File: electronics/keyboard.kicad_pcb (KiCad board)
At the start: 2 copper layers, 169 parts, among them J1 CONN_02X10, SW1 SW_Push, SW10 SW_Push, SW11 SW_Push, SW12 SW_Push, SW13 SW_Push, SW14 SW_Push, SW15 SW_Push, SW16 SW_Push, SW17 SW_Push, SW18 SW_Push, SW19 SW_Push, SW20 SW_Push, SW21 SW_Push, SW22 SW_Push, SW23 SW_Push, SW24 SW_Push, SW25 SW_Push, SW27 SW_Push, SW28 SW_Push, SW29 SW_Push, SW3 SW_Push, SW30 SW_Push, SW31 SW_Push, SW32 SW_Push, SW33 SW_Push, SW34 SW_Push, SW35 SW_Push, SW36 SW_Push, SW37 SW_Push, SW38 SW_Push, SW39 SW_Push, SW4 SW_Push, SW40 SW_Push, SW41 SW_Push, SW42 SW_Push, SW43 SW_Push, SW44 SW_Push, SW45 SW_Push, SW46 SW_Push, SW47 SW_Push, SW48 SW_Push, SW49 SW_Push, SW5 SW_Push, SW50 SW_Push, SW51 SW_Push, SW52 SW_Push, SW53 SW_Push, SW54 SW_Push, SW55 SW_Push, SW56 SW_Push, SW57 SW_Push, SW58 SW_Push, SW59 SW_Push, SW6 SW_Push, SW60 SW_Push, SW61 SW_Push, SW62 SW_Push, SW63 SW_Push, SW64 SW_Push, SW65 SW_Push, SW66 SW_Push, SW67 SW_Push, SW68 SW_Push, SW69 SW_Push, SW7 SW_Push, SW70 SW_Push, SW71 SW_Push, SW72 SW_Push, SW73 SW_Push, SW74 SW_Push, SW75 SW_Push, SW76 SW_Push, SW77 SW_Push, SW78 SW_Push, SW8 SW_Push, SW81 SW_Push, SW82 SW_Push, SW83 SW_Push, SW84 SW_Push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

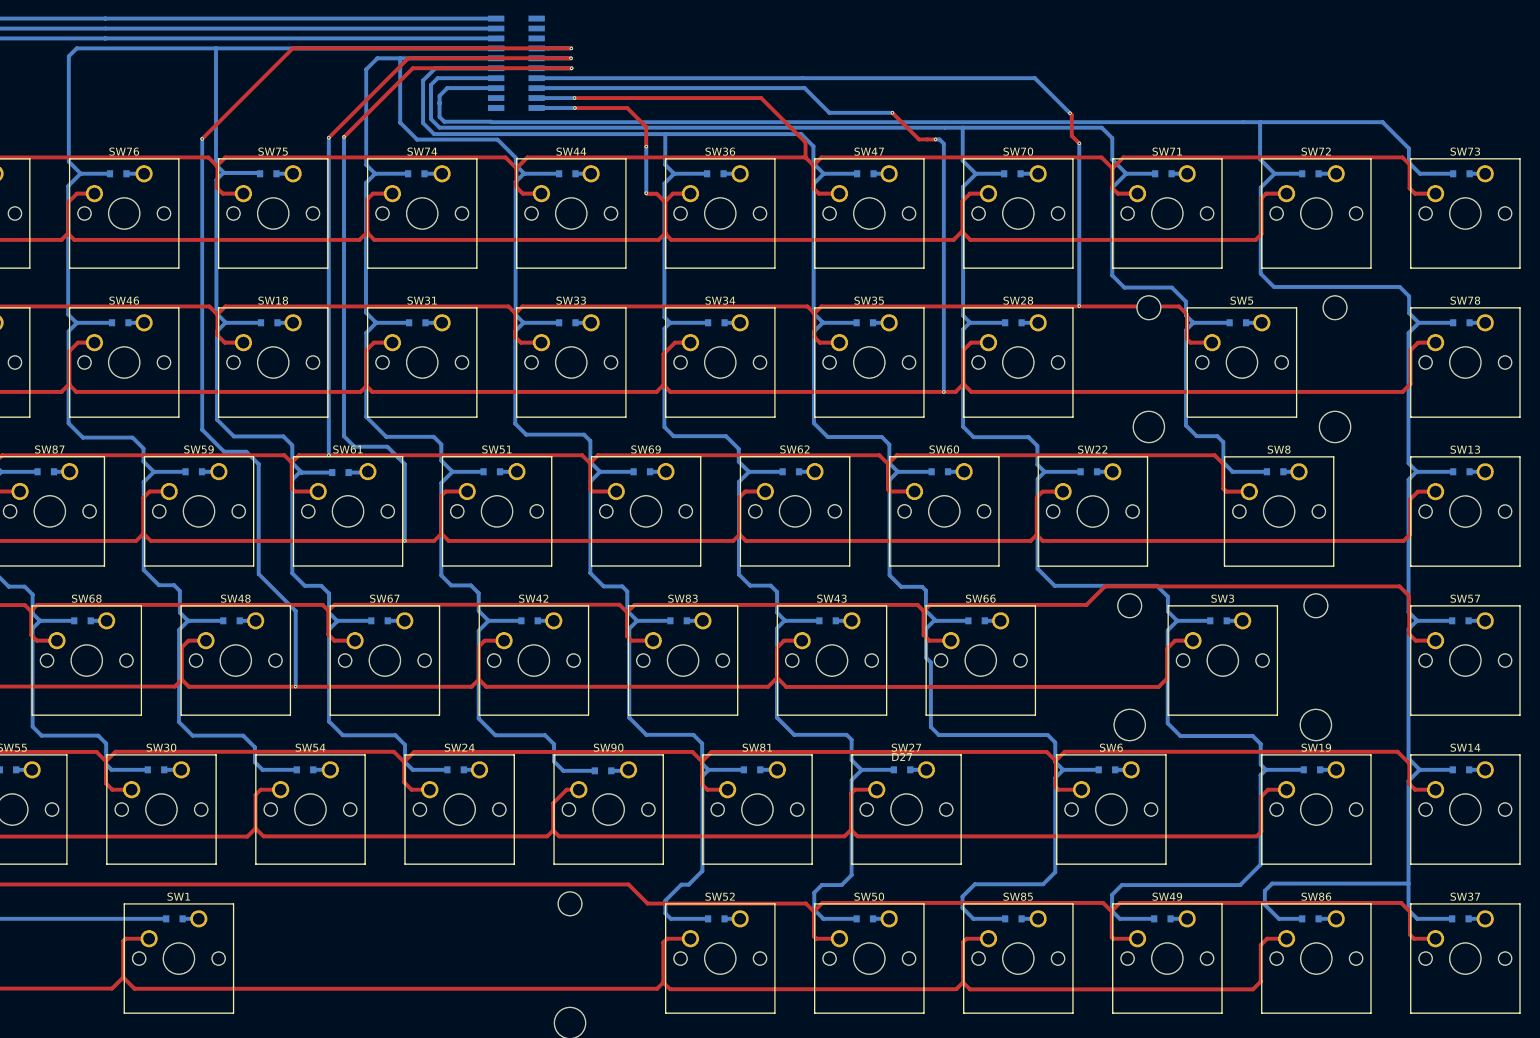
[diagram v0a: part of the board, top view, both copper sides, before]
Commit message: Initial complete signal routing of the connector
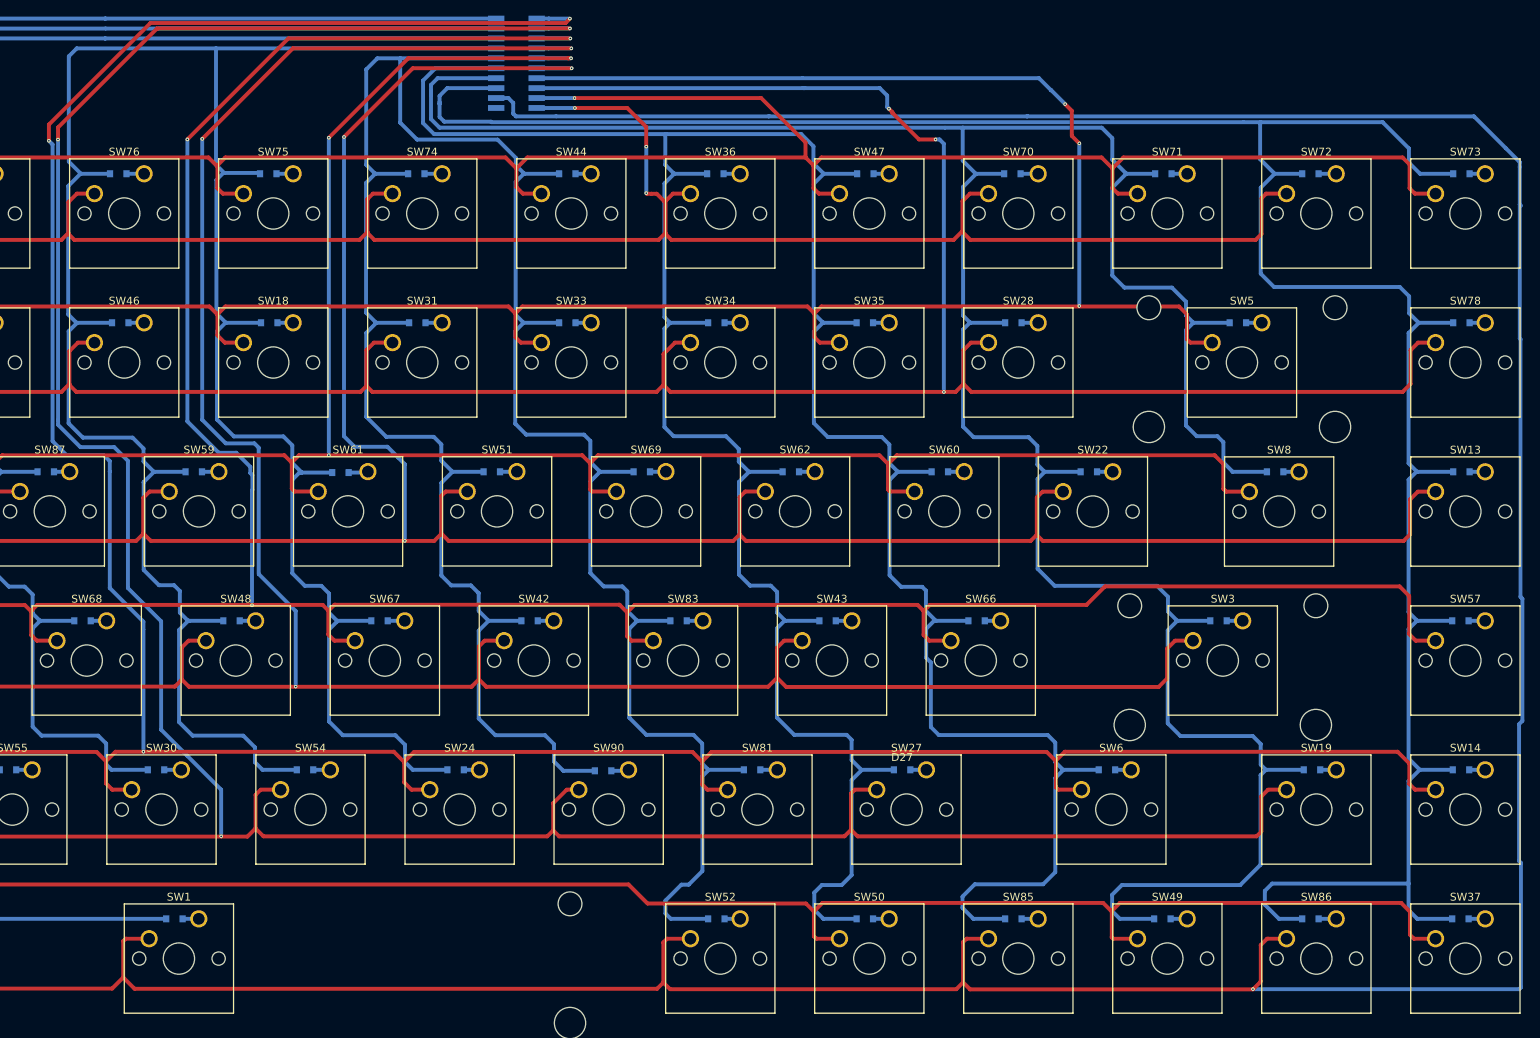
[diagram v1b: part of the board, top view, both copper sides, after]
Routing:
- net /PC2: track 318.7 -> 594.3 mm, vias 0 -> 1
- net /PC0: track 313.9 -> 490.7 mm, vias 0 -> 3
- net /PC1: track 294.9 -> 459.3 mm, vias 0 -> 3
- net /PB7: track 306.4 -> 429.4 mm, vias 0 -> 3
- net /PB2: track 442.0 -> 443.1 mm

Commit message: Fixed strange drc errors with replacing vias
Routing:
- net /PB2: track 443.1 -> 447.2 mm
- net Net-(D58-Pad2): track 0.00 -> 2.01 mm
- net /PA0: track 545.5 -> 547.5 mm
- net /PC0: track 490.7 -> 492.3 mm
- net /PB7: track 429.4 -> 430.2 mm
- net /PB6: track 438.8 -> 439.5 mm
- net /PC1: track 459.3 -> 459.9 mm

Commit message: Added outline and some drill holes
todo:
    - Additional 2 drill holes
    - update fill zones
    - add led for shift switch
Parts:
- added REF**: MountingHole_3.2mm_M3, Mounting_Holes:MountingHole_3.2mm_M3, F.Cu at (34.9, 228.0)
- added REF**: MountingHole_3.2mm_M3, Mounting_Holes:MountingHole_3.2mm_M3, F.Cu at (320.9, 228.0)
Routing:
- net /PA1: track 465.7 -> 456.9 mm
- added copper zone on B.Cu, net (none)
- added copper zone on F.Cu, net (none)
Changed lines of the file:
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@@
 (kicad_pcb (version 4) (host pcbnew 4.0.6)
   (general
-    (links 251)
-    (no_connects 1)
-    (area 25.703749 90 331.110001 225.07)
+    (links 0)
+    (no_connects 0)
+    (area 25.350857 89.714399 331.110001 234.128001)
     (thickness 1.6)
-    (drawings 1853)
+    (drawings 1856)
     (tracks 1422)
     (zones 0)
-    (modules 169)
+    (modules 171)
     (nets 106)
   )
@@
     (33 F.Adhes user)
     (34 B.Paste user)
-    (35 F.Paste user)
+    (35 F.Paste user hide)
     (36 B.SilkS user)
     (37 F.SilkS user)
@@
     (pad_drill 0.762)
     (pad_to_mask_clearance 0.2)
-    (aux_axis_origin 0 0)
-    (visible_elements FFFFF77F)
+    (aux_axis_origin 25.908 224.028)
+    (grid_origin 25.908 224.028)
+    (visible_elements FFFFFFFF)
     (pcbplotparams
       (layerselection 0x00030_80000001)
@@
     (add_net "Net-(D90-Pad2)")
   )
+  (module Mounting_Holes:MountingHole_3.2mm_M3 (layer F.Cu)
+    (at 34.908 228.028)
+    (descr "Mounting Hole 3.2mm, no annular, M3")
+    (tags "mounting hole 3.2mm no annular m3")
+    (fp_text reference REF** (at 0 -4.2) (layer F.SilkS)
+      (effects (font (size 1 1) (thickness 0.15)))
+    )
+    (fp_text value MountingHole_3.2mm_M3 (at 0 4.2) (layer F.Fab)
+      (effects (font (size 1 1) (thickness 0.15)))
+    )
+    (fp_circle (center 0 0) (end 3.2 0) (layer Cmts.User) (width 0.15))
+    (fp_circle (center 0 0) (end 3.45 0) (layer F.CrtYd) (width 0.05))
+    (pad 1 np_thru_hole circle (at 0 0) (size 3.2 3.2) (drill 3.2) (layers *.Cu *.Mask))
+  )
   (module Diodes_SMD:D_0805 (layer B.Cu)
     (at 42.037 171.45)
@@
     )
   )
+  (module Mounting_Holes:MountingHole_3.2mm_M3 (layer F.Cu)
+    (at 320.908 228.028)
+    (descr "Mounting Hole 3.2mm, no annular, M3")
+    (tags "mounting hole 3.2mm no annular m3")
+    (fp_text reference REF** (at 0 -4.2) (layer F.SilkS)
+      (effects (font (size 1 1) (thickness 0.15)))
+    )
+    (fp_text value MountingHole_3.2mm_M3 (at 0 4.2) (layer F.Fab)
+      (effects (font (size 1 1) (thickness 0.15)))
+    )
+    (fp_circle (center 0 0) (end 3.2 0) (layer Cmts.User) (width 0.15))
+    (fp_circle (center 0 0) (end 3.45 0) (layer F.CrtYd) (width 0.05))
+    (pad 1 np_thru_hole circle (at 0 0) (size 3.2 3.2) (drill 3.2) (layers *.Cu *.Mask))
+  )
+  (gr_line (start 330.908 234.028) (end 330.908 224.028) (layer Dwgs.User) (width 0.2))
+  (gr_line (start 25.908 234.028) (end 330.908 234.028) (layer Dwgs.User) (width 0.2))
+  (gr_line (start 25.908 224.028) (end 25.908 234.028) (layer Dwgs.User) (width 0.2))
   (gr_line (start 330.8096 224.14992) (end 330.8096 224.14992) (layer Dwgs.User) (width 0.2))
   (gr_line (start 330.8096 104.9528) (end 330.8096 224.14992) (layer Dwgs.User) (width 0.2))
@@
   (segment (start 45.0342 94.4626) (end 44.9326 94.4626) (width 0.5) (layer B.Cu) (net 4))
   (segment (start 43.087 171.45) (end 45.2 171.45) (width 0.5) (layer B.Cu) (net 5))
+  (segment (start 80.908 208.028) (end 82.43 209.55) (width 0.5) (layer B.Cu) (net 6))
+  (segment (start 82.43 209.55) (end 83.913 209.55) (width 0.5) (layer B.Cu) (net 6))
+  (segment (start 80.908 206.028) (end 80.908 208.028) (width 0.5) (layer B.Cu) (net 6))
+  (segment (start 81.7548 205.1812) (end 80.908 206.028) (width 0.5) (layer B.Cu) (net 6))
+  (segment (start 84.8106 205.1812) (end 81.7548 205.1812) (width 0.5) (layer B.Cu) (net 6))
   (segment (start 91.152 114.3) (end 84.9376 114.3) (width 0.5) (layer B.Cu) (net 6))
   (segment (start 197.415 95.7326) (end 147.4782 95.7326) (width 0.5) (layer B.Cu) (net 6))
@@
   (segment (start 84.8614 114.3) (end 83.1596 112.5982) (width 0.5) (layer B.Cu) (net 6))
   (segment (start 89.6366 190.5) (end 89.5858 190.5) (width 0.5) (layer B.Cu) (net 6))
-  (segment (start 78.1304 209.55) (end 83.913 209.55) (width 0.5) (layer B.Cu) (net 6))
-  (segment (start 76.4286 207.8482) (end 78.1304 209.55) (width 0.5) (layer B.Cu) (net 6))
-  (segment (start 76.4286 206.0702) (end 76.4286 207.8482) (width 0.5) (layer B.Cu) (net 6))
-  (segment (start 77.3176 205.1812) (end 76.4286 206.0702) (width 0.5) (layer B.Cu) (net 6))
-  (segment (start 84.8106 205.1812) (end 77.3176 205.1812) (width 0.5) (layer B.Cu) (net 6))
   (segment (start 87.8586 202.1332) (end 84.8106 205.1812) (width 0.5) (layer B.Cu) (net 6))
   (segment (start 87.8586 192.2272) (end 87.8586 202.1332) (width 0.5) (layer B.Cu) (net 6))
@@
   (segment (start 238.0234 211.7852) (end 238.3282 212.09) (width 0.5) (layer F.Cu) (net 104))
   (segment (start 238.3282 212.09) (end 241.3 212.09) (width 0.5) (layer F.Cu) (net 104))
+  (zone (net 0) (net_name "") (layer B.Cu) (hatch edge 0.508)
+    (connect_pads (clearance 0.508))
+    (min_thickness 0.254)
+    (fill (arc_segments 16) (thermal_gap 0.508) (thermal_bridge_width 0.508))
+    (polygon
+      (pts
+        (xy 25.908 105.156) (xy 41.148 89.916) (xy 315.468 89.916) (xy 315.722 89.916) (xy 330.708 104.902)
+        (xy 330.708 224.028) (xy 25.908 223.774)
+      )
+    )
+  )
+  (zone (net 0) (net_name "") (layer F.Cu) (hatch edge 0.508)
+    (connect_pads (clearance 0.508))
+    (min_thickness 0.254)
+    (fill (arc_segments 16) (thermal_gap 0.508) (thermal_bridge_width 0.508))
+    (polygon
+      (pts
+        (xy 25.908 223.774) (xy 25.908 105.156) (xy 41.148 89.916) (xy 315.722 89.916) (xy 330.708 104.902)
+        (xy 330.708 224.028) (xy 25.908 224.028)
+      )
+    )
+  )
 )

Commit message: updated pcb
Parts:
- moved REF** 1.00 mm to (35.9, 228.0)
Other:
- net class Default: via_dia 0.45 -> 0.6; via_drill 0.2 -> 0.3
- net class Double: via_dia 0.45 -> 0.6; via_drill 0.2 -> 0.3
- rule via_min_drill: 0.2 -> 0.3
- rule via_min_size: 0.45 -> 0.6
- board text added: "Change min Via"
- board text added: "LED Shift taste"
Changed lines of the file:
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@@
     (links 0)
     (no_connects 0)
-    (area 25.350857 89.714399 331.110001 234.128001)
+    (area 25.703749 89.714399 360.472286 250.728001)
     (thickness 1.6)
-    (drawings 1856)
+    (drawings 1860)
     (tracks 1422)
     (zones 0)
@@
     (segment_width 0.2)
     (edge_width 0.15)
-    (via_size 0.45)
-    (via_drill 0.2)
-    (via_min_size 0.45)
-    (via_min_drill 0.2)
+    (via_size 0.6)
+    (via_drill 0.3)
+    (via_min_size 0.6)
+    (via_min_drill 0.3)
     (uvia_size 0.3)
     (uvia_drill 0.1)
@@
     (clearance 0.2)
     (trace_width 0.25)
-    (via_dia 0.45)
-    (via_drill 0.2)
+    (via_dia 0.6)
+    (via_drill 0.3)
     (uvia_dia 0.3)
     (uvia_drill 0.1)
@@
     (clearance 0.2)
     (trace_width 0.5)
-    (via_dia 0.45)
-    (via_drill 0.2)
+    (via_dia 0.6)
+    (via_drill 0.3)
     (uvia_dia 0.3)
     (uvia_drill 0.1)
@@
   )
   (module Mounting_Holes:MountingHole_3.2mm_M3 (layer F.Cu)
-    (at 34.908 228.028)
+    (at 35.908 228.028)
     (descr "Mounting Hole 3.2mm, no annular, M3")
     (tags "mounting hole 3.2mm no annular m3")
@@
     (pad 1 np_thru_hole circle (at 0 0) (size 3.2 3.2) (drill 3.2) (layers *.Cu *.Mask))
   )
+  (gr_text "Change min Via " (at 59.908 237.028) (layer Dwgs.User)
+    (effects (font (size 3 3) (thickness 0.3)))
+  )
+  (dimension 144 (width 0.3) (layer Dwgs.User)
+    (gr_text "144.000 mm" (at 353.258 162.028 90) (layer Dwgs.User)
+      (effects (font (size 1.5 1.5) (thickness 0.3)))
+    )
+    (feature1 (pts (xy 337.908 90.028) (xy 354.608 90.028)))
+    (feature2 (pts (xy 337.908 234.028) (xy 354.608 234.028)))
+    (crossbar (pts (xy 351.908 234.028) (xy 351.908 90.028)))
+    (arrow1a (pts (xy 351.908 90.028) (xy 352.494421 91.154504)))
+    (arrow1b (pts (xy 351.908 90.028) (xy 351.321579 91.154504)))
+    (arrow2a (pts (xy 351.908 234.028) (xy 352.494421 232.901496)))
+    (arrow2b (pts (xy 351.908 234.028) (xy 351.321579 232.901496)))
+  )
+  (dimension 305 (width 0.3) (layer Dwgs.User)
+    (gr_text "305.000 mm" (at 178.408 249.378) (layer Dwgs.User)
+      (effects (font (size 1.5 1.5) (thickness 0.3)))
+    )
+    (feature1 (pts (xy 330.908 244.028) (xy 330.908 250.728)))
+    (feature2 (pts (xy 25.908 244.028) (xy 25.908 250.728)))
+    (crossbar (pts (xy 25.908 248.028) (xy 330.908 248.028)))
+    (arrow1a (pts (xy 330.908 248.028) (xy 329.781496 248.614421)))
+    (arrow1b (pts (xy 330.908 248.028) (xy 329.781496 247.441579)))
+    (arrow2a (pts (xy 25.908 248.028) (xy 27.034504 248.614421)))
+    (arrow2b (pts (xy 25.908 248.028) (xy 27.034504 247.441579)))
+  )
+  (gr_text "LED Shift taste\n" (at 57.908 228.028) (layer Dwgs.User)
+    (effects (font (size 3 3) (thickness 0.3)))
+  )
   (gr_line (start 330.908 234.028) (end 330.908 224.028) (layer Dwgs.User) (width 0.2))
   (gr_line (start 25.908 234.028) (end 330.908 234.028) (layer Dwgs.User) (width 0.2))
@@
   (segment (start 186.436 100.98024) (end 177.95748 109.45876) (width 0.5) (layer F.Cu) (net 96))
   (segment (start 186.83224 100.584) (end 186.436 100.98024) (width 0.5) (layer F.Cu) (net 96))
-  (via (at 206.756 100.584) (size 0.45) (drill 0.2) (layers F.Cu B.Cu) (net 96))
+  (via (at 206.756 100.584) (size 0.6) (drill 0.3) (layers F.Cu B.Cu) (net 96))
   (segment (start 206.5274 100.8126) (end 206.756 100.584) (width 0.5) (layer B.Cu) (net 96))
   (segment (start 202.585 100.8126) (end 206.5274 100.8126) (width 0.5) (layer B.Cu) (net 96))
@@
   (segment (start 154.2796 95.504) (end 153.7716 96.012) (width 0.5) (layer F.Cu) (net 100))
   (segment (start 206.756 95.504) (end 154.2796 95.504) (width 0.5) (layer F.Cu) (net 100))
-  (via (at 206.756 95.504) (size 0.45) (drill 0.2) (layers F.Cu B.Cu) (net 100))
+  (via (at 206.756 95.504) (size 0.6) (drill 0.3) (layers F.Cu B.Cu) (net 100))
   (segment (start 206.5274 95.7326) (end 206.756 95.504) (width 0.5) (layer B.Cu) (net 100))
   (segment (start 202.585 95.7326) (end 206.5274 95.7326) (width 0.5) (layer B.Cu) (net 100))
@@
   (segment (start 206.488602 94.44736) (end 153.797 94.44736) (width 0.5) (layer F.Cu) (net 101))
   (segment (start 153.797 94.44736) (end 140.22832 108.01604) (width 0.5) (layer F.Cu) (net 101))
-  (via (at 206.8322 94.47276) (size 0.45) (drill 0.2) (layers F.Cu B.Cu) (net 101))
+  (via (at 206.908 94.47276) (size 0.6) (drill 0.3) (layers F.Cu B.Cu) (net 101))
   (segment (start 204.14516 94.47276) (end 206.8322 94.47276) (width 0.5) (layer B.Cu) (net 101))
   (segment (start 202.585 94.4626) (end 204.135 94.4626) (width 0.5) (layer B.Cu) (net 101))

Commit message: Update keyboard.kicad_pcb
Updated Via size
Fixed fill area size

Todo:
- 2 additional drill holes
- led for shift
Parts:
- moved REF** 0.16 mm to (36.1, 228.0)
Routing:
- net /PA0: track 547.5 -> 566.1 mm
